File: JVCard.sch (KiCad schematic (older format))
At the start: 75 parts, among them J6 Conn_02x25_Odd_Even, Q1 mmbt3904, Q2 mmbt3904, Q3 mmbt3904, Q4 mmbt3904, Q5 mmbt3904, Q6 mmbt3904, U1 AMS1117-5.0, U4 SCART_CONN

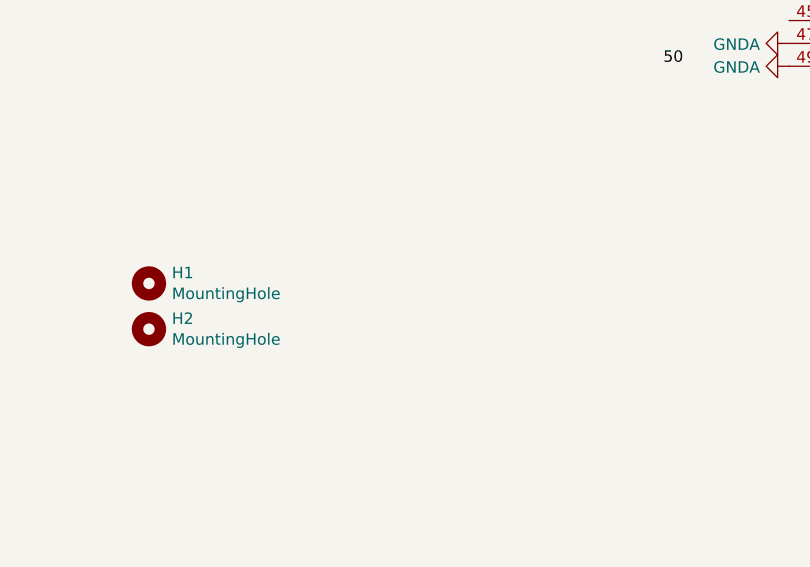
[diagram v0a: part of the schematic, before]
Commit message: add rear panel
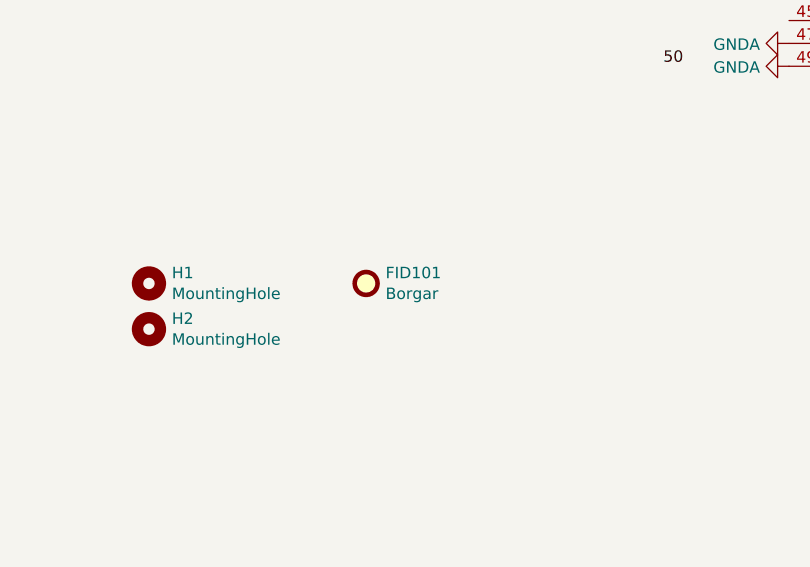
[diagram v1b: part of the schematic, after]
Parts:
- added FID101: Borgar, videobits:borgar, symbol Mechanical:Fiducial
- U1: LCSC (none) -> C6187
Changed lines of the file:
@@
 F 2 "Package_TO_SOT_SMD:SOT-223-3_TabPin2" H 2650 6850 50  0001 C CNN
 F 3 "http://www.advanced-monolithic.com/pdf/ds1117.pdf" H 2750 6400 50  0001 C CNN
+F 4 "C6187" H 2650 6650 50  0001 C CNN "LCSC"
 	1    2650 6650
 	1    0    0    -1
 $EndComp
 Connection ~ 2950 6650
+$Comp
+L Mechanical:Fiducial FID101
+U 1 1 5EC7B9E1
+P 8650 5400
+F 0 "FID101" H 8735 5446 50  0000 L CNN
+F 1 "Borgar" H 8735 5355 50  0000 L CNN
+F 2 "videobits:borgar" H 8650 5400 50  0001 C CNN
+F 3 "~" H 8650 5400 50  0001 C CNN
+	1    8650 5400
+	1    0    0    -1
+$EndComp
 $EndSCHEMATC
